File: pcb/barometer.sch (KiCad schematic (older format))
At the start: 3 parts, among them IC703 MS5611-01BA03

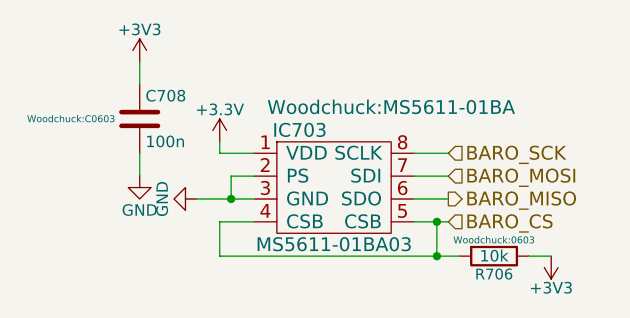
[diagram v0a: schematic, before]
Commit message: Generated net list (only two footprints remaining), added a few footprints, started rough estimate of PCB size
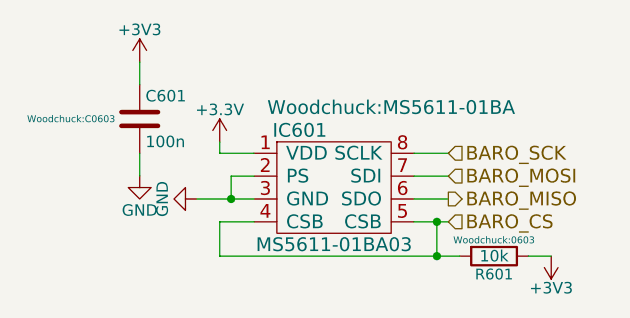
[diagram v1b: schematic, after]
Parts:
- renumbered C708 to C601, IC703 to IC601, R706 to R601
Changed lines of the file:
@@
 $EndDescr
 $Comp
-L MS5611-01BA03 IC703
+L MS5611-01BA03 IC601
 U 1 1 565CC16E
 P 3350 2050
-F 0 "IC703" H 3200 2250 60  0000 C CNN
+F 0 "IC601" H 3200 2250 60  0000 C CNN
 F 1 "MS5611-01BA03" H 3350 1750 60  0000 C CNN
 F 2 "Woodchuck:MS5611-01BA" H 3600 2350 60  0000 C CNN
@@
 Connection ~ 3800 2400
 $Comp
-L R R706
+L R R601
 U 1 1 565D7136
 P 4050 2400
-F 0 "R706" V 4130 2400 47  0000 C CNN
+F 0 "R601" V 4130 2400 47  0000 C CNN
 F 1 "10k" V 4050 2400 50  0000 C CNN
 F 2 "Woodchuck:0603" V 3980 2400 30  0000 C CNN
@@
 $EndComp
 $Comp
-L +3.3V #PWR30
+L +3.3V #PWR032
 U 1 1 565D7402
 P 2850 1900
-F 0 "#PWR30" H 2850 1750 50  0001 C CNN
+F 0 "#PWR032" H 2850 1750 50  0001 C CNN
 F 1 "+3.3V" H 2850 2040 50  0000 C CNN
 F 2 "" H 2850 1900 60  0000 C CNN
@@
 $EndComp
 $Comp
-L GND #PWR29
+L GND #PWR033
 U 1 1 565D746E
 P 2750 2150
-F 0 "#PWR29" H 2750 1900 50  0001 C CNN
+F 0 "#PWR033" H 2750 1900 50  0001 C CNN
 F 1 "GND" H 2750 2000 50  0000 C CNN
 F 2 "" H 2750 2150 60  0000 C CNN
@@
 $EndComp
 $Comp
-L GND #PWR28
+L GND #PWR034
 U 1 1 565D7486
 P 2500 2050
-F 0 "#PWR28" H 2500 1800 50  0001 C CNN
+F 0 "#PWR034" H 2500 1800 50  0001 C CNN
 F 1 "GND" H 2500 1900 50  0000 C CNN
 F 2 "" H 2500 2050 60  0000 C CNN
@@
 Connection ~ 2900 2150
 $Comp
-L C C708
+L C C601
 U 1 1 565D7512
 P 2500 1800
-F 0 "C708" H 2525 1900 50  0000 L CNN
+F 0 "C601" H 2525 1900 50  0000 L CNN
 F 1 "100n" H 2525 1700 50  0000 L CNN
 F 2 "Woodchuck:C0603" H 2200 1800 30  0000 C CNN
@@
 	2500 1550 2500 1650
 $Comp
-L +3V3 #PWR31
+L +3V3 #PWR035
 U 1 1 565D777C
 P 4300 2400
-F 0 "#PWR31" H 4300 2250 50  0001 C CNN
+F 0 "#PWR035" H 4300 2250 50  0001 C CNN
 F 1 "+3V3" H 4300 2540 50  0000 C CNN
 F 2 "" H 4300 2400 60  0000 C CNN
@@
 	4200 2400 4300 2400
 $Comp
-L +3V3 #PWR27
+L +3V3 #PWR036
 U 1 1 565D78F9
 P 2500 1550
-F 0 "#PWR27" H 2500 1400 50  0001 C CNN
+F 0 "#PWR036" H 2500 1400 50  0001 C CNN
 F 1 "+3V3" H 2500 1690 50  0000 C CNN
 F 2 "" H 2500 1550 60  0000 C CNN

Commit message: Fix barometer hierarchical pins and add Farnell numbers to components
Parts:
- C601: Farnell Value -> 9406140
- IC601: Digikey (none) -> Value; Farnell (none) -> 2362662; Fieldname (none) -> Value
- R601: Digikey (none) -> Value; Farnell (none) -> 9331700; Fieldname (none) -> Value
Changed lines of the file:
@@
 F 2 "Woodchuck:MS5611-01BA" H 3600 2350 60  0000 C CNN
 F 3 "" H 3350 2050 60  0000 C CNN
+F 4 "Value" H 3350 2050 60  0001 C CNN "Digikey"
+F 5 "2362662" H 3350 2050 60  0001 C CNN "Farnell"
+F 6 "Value" H 3350 2050 60  0001 C CNN "Fieldname"
 	1    3350 2050
 	1    0    0    -1
@@
 F 2 "Woodchuck:0603" V 3980 2400 30  0000 C CNN
 F 3 "" H 4050 2400 30  0000 C CNN
+F 4 "Value" H 4050 2400 60  0001 C CNN "Digikey"
+F 5 "9331700" H 4050 2400 60  0001 C CNN "Farnell"
+F 6 "Value" H 4050 2400 60  0001 C CNN "Fieldname"
 	1    4050 2400
 	0    1    1    0
 $EndComp
 $Comp
-L +3.3V #PWR032
+L +3.3V #PWR030
 U 1 1 565D7402
 P 2850 1900
-F 0 "#PWR032" H 2850 1750 50  0001 C CNN
+F 0 "#PWR030" H 2850 1750 50  0001 C CNN
 F 1 "+3.3V" H 2850 2040 50  0000 C CNN
 F 2 "" H 2850 1900 60  0000 C CNN
@@
 $EndComp
 $Comp
-L GND #PWR033
+L GND #PWR031
 U 1 1 565D746E
 P 2750 2150
-F 0 "#PWR033" H 2750 1900 50  0001 C CNN
+F 0 "#PWR031" H 2750 1900 50  0001 C CNN
 F 1 "GND" H 2750 2000 50  0000 C CNN
 F 2 "" H 2750 2150 60  0000 C CNN
@@
 $EndComp
 $Comp
-L GND #PWR034
+L GND #PWR032
 U 1 1 565D7486
 P 2500 2050
-F 0 "#PWR034" H 2500 1800 50  0001 C CNN
+F 0 "#PWR032" H 2500 1800 50  0001 C CNN
 F 1 "GND" H 2500 1900 50  0000 C CNN
 F 2 "" H 2500 2050 60  0000 C CNN
@@
 F 3 "" H 2500 1800 60  0000 C CNN
 F 4 "Value" H 2500 1800 60  0001 C CNN "Digikey"
-F 5 "Value" H 2500 1800 60  0001 C CNN "Farnell"
+F 5 "9406140" H 2500 1800 60  0001 C CNN "Farnell"
 F 6 "Value" H 2500 1800 60  0001 C CNN "Fieldname"
 	1    2500 1800
@@
 	2500 1550 2500 1650
 $Comp
-L +3V3 #PWR035
+L +3V3 #PWR033
 U 1 1 565D777C
 P 4300 2400
-F 0 "#PWR035" H 4300 2250 50  0001 C CNN
+F 0 "#PWR033" H 4300 2250 50  0001 C CNN
 F 1 "+3V3" H 4300 2540 50  0000 C CNN
 F 2 "" H 4300 2400 60  0000 C CNN
@@
 	4200 2400 4300 2400
 $Comp
-L +3V3 #PWR036
+L +3V3 #PWR034
 U 1 1 565D78F9
 P 2500 1550
-F 0 "#PWR036" H 2500 1400 50  0001 C CNN
+F 0 "#PWR034" H 2500 1400 50  0001 C CNN
 F 1 "+3V3" H 2500 1690 50  0000 C CNN
 F 2 "" H 2500 1550 60  0000 C CNN

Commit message: Fixed some errors in the schematics
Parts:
- C601: Farnell 9406140 -> 1759037
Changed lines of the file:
@@
 $Descr A4 11693 8268
 encoding utf-8
-Sheet 6 6
+Sheet 5 5
 Title ""
 Date ""
@@
 F 3 "" H 2500 1800 60  0000 C CNN
 F 4 "Value" H 2500 1800 60  0001 C CNN "Digikey"
-F 5 "9406140" H 2500 1800 60  0001 C CNN "Farnell"
+F 5 "1759037" H 2500 1800 60  0001 C CNN "Farnell"
 F 6 "Value" H 2500 1800 60  0001 C CNN "Fieldname"
 	1    2500 1800

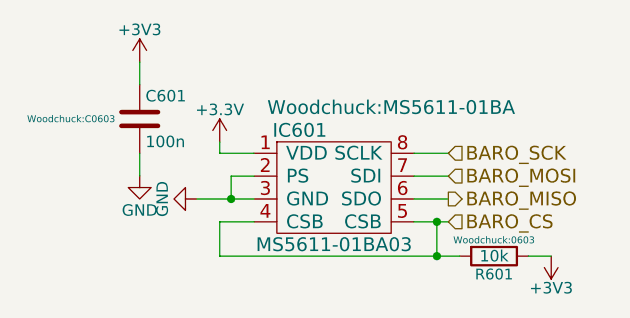
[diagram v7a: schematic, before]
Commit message: Hide footprints on schematic, fix overlaps
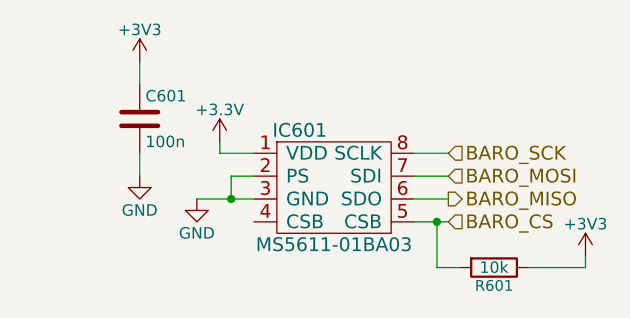
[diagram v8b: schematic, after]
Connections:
- net BARO_CS: no longer IC601.4 (CSB)
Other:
- moved on the sheet: R601
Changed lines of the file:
@@
 F 0 "IC601" H 3200 2250 60  0000 C CNN
 F 1 "MS5611-01BA03" H 3350 1750 60  0000 C CNN
-F 2 "Woodchuck:MS5611-01BA" H 3600 2350 60  0000 C CNN
+F 2 "Woodchuck:MS5611-01BA" H 3600 2350 60  0001 C CNN
 F 3 "http://www.daedalus.ei.tum.de/attachments/article/61/MS5611-01BA01.pdf" H 3350 2050 60  0001 C CNN
 F 4 "Value" H 3350 2050 60  0001 C CNN "Digikey"
@@
 BARO_CS
 Wire Wire Line
-	3700 2250 3850 2250
+	3700 2250 3800 2250
 Wire Wire Line
-	3000 2250 2850 2250
+	3800 2250 3850 2250
 Wire Wire Line
-	2850 2250 2850 2400
+	3800 2450 3900 2450
 Wire Wire Line
-	2850 2400 3900 2400
-Wire Wire Line
-	3800 2400 3800 2250
+	3800 2450 3800 2250
 Connection ~ 3800 2250
-Connection ~ 3800 2400
 $Comp
 L R R601
 U 1 1 565D7136
-P 4050 2400
-F 0 "R601" V 4130 2400 47  0000 C CNN
-F 1 "10k" V 4050 2400 50  0000 C CNN
-F 2 "Woodchuck:0603" V 3980 2400 30  0000 C CNN
-F 3 "" H 4050 2400 30  0000 C CNN
-F 4 "Value" H 4050 2400 60  0001 C CNN "Digikey"
-F 5 "9331700" H 4050 2400 60  0001 C CNN "Farnell"
-F 6 "Value" H 4050 2400 60  0001 C CNN "Fieldname"
-	1    4050 2400
+P 4050 2450
+F 0 "R601" V 4130 2450 47  0000 C CNN
+F 1 "10k" V 4050 2450 50  0000 C CNN
+F 2 "Woodchuck:0603" V 3980 2450 30  0001 C CNN
+F 3 "" H 4050 2450 30  0000 C CNN
+F 4 "Value" H 4050 2450 60  0001 C CNN "Digikey"
+F 5 "9331700" H 4050 2450 60  0001 C CNN "Farnell"
+F 6 "Value" H 4050 2450 60  0001 C CNN "Fieldname"
+	1    4050 2450
 	0    1    1    0
 $EndComp
@@
 F 3 "" H 2750 2150 60  0000 C CNN
 	1    2750 2150
-	0    1    1    0
+	1    0    0    -1
 $EndComp
 $Comp
@@
 	2850 1950 2850 1900
 Wire Wire Line
-	2750 2150 3000 2150
+	2750 2150 2900 2150
+Wire Wire Line
+	2900 2150 3000 2150
 Wire Wire Line
 	3000 2050 2900 2050
@@
 F 0 "C601" H 2525 1900 50  0000 L CNN
 F 1 "100n" H 2525 1700 50  0000 L CNN
-F 2 "Woodchuck:C0603" H 2200 1800 30  0000 C CNN
+F 2 "Woodchuck:C0603" H 2200 1800 30  0001 C CNN
 F 3 "" H 2500 1800 60  0000 C CNN
 F 4 "Value" H 2500 1800 60  0001 C CNN "Digikey"
@@
 L +3V3 #PWR505
 U 1 1 565D777C
-P 4300 2400
-F 0 "#PWR505" H 4300 2250 50  0001 C CNN
-F 1 "+3V3" H 4300 2540 50  0000 C CNN
-F 2 "" H 4300 2400 60  0000 C CNN
-F 3 "" H 4300 2400 60  0000 C CNN
-	1    4300 2400
-	-1   0    0    1
+P 4450 2400
+F 0 "#PWR505" H 4450 2250 50  0001 C CNN
+F 1 "+3V3" H 4450 2540 50  0000 C CNN
+F 2 "" H 4450 2400 60  0000 C CNN
+F 3 "" H 4450 2400 60  0000 C CNN
+	1    4450 2400
+	1    0    0    -1
 $EndComp
 Wire Wire Line
-	4200 2400 4300 2400
+	4200 2450 4450 2450
 $Comp
 L +3V3 #PWR501
@@
 	1    0    0    -1
 $EndComp
+Wire Wire Line
+	4450 2450 4450 2400
 $EndSCHEMATC
